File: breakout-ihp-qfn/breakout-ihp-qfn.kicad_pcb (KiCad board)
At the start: 4 copper layers, 50 x 50 mm, 113 parts, among them J1 Conn_01x12, J2 DF12NB-60DS-0.5V_51, J3 DF12NB-50DS-0.5V_51, U1 AP2112K-1.2, U2 AP2112K-1.8, U3 TT_IHP_ASIC, U4 24LC02

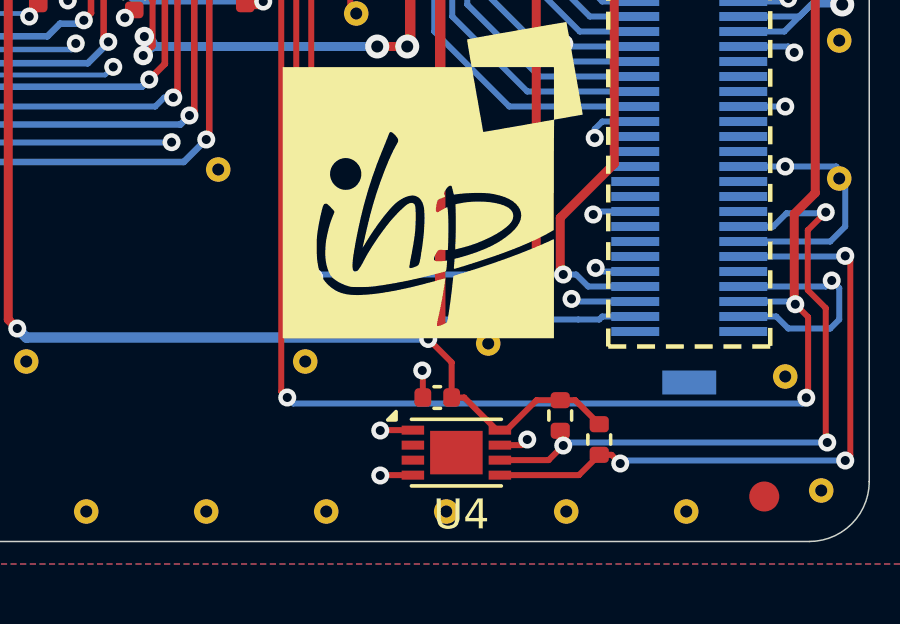
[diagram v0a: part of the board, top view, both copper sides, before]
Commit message: schem cleanup/project mux bus renames
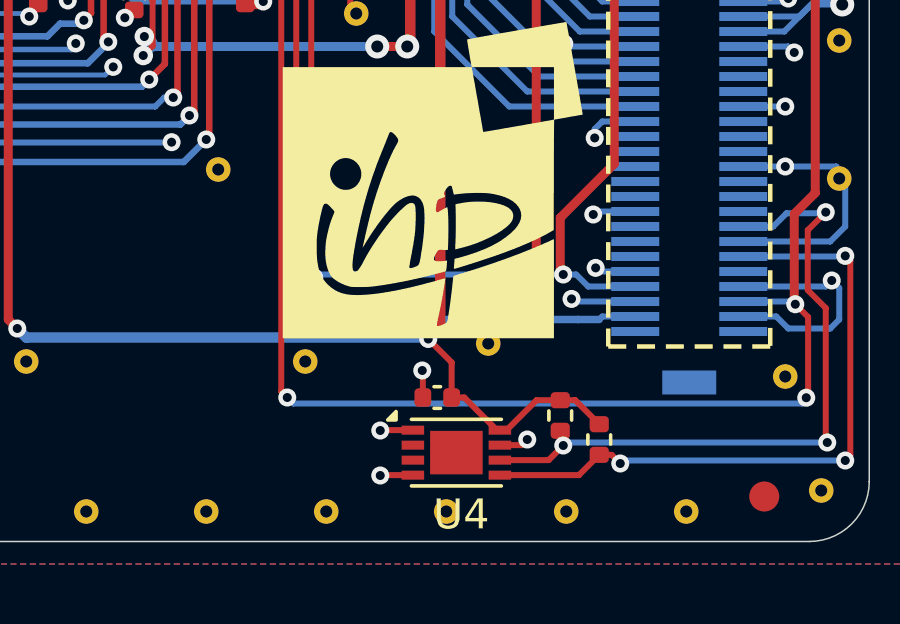
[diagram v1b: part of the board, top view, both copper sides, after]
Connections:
- net /c_ena renamed /enable
- net /c_rst_n renamed /rst_n
- net /c_sel_inc renamed /increment
- net /p_rst renamed /~{p_rst}

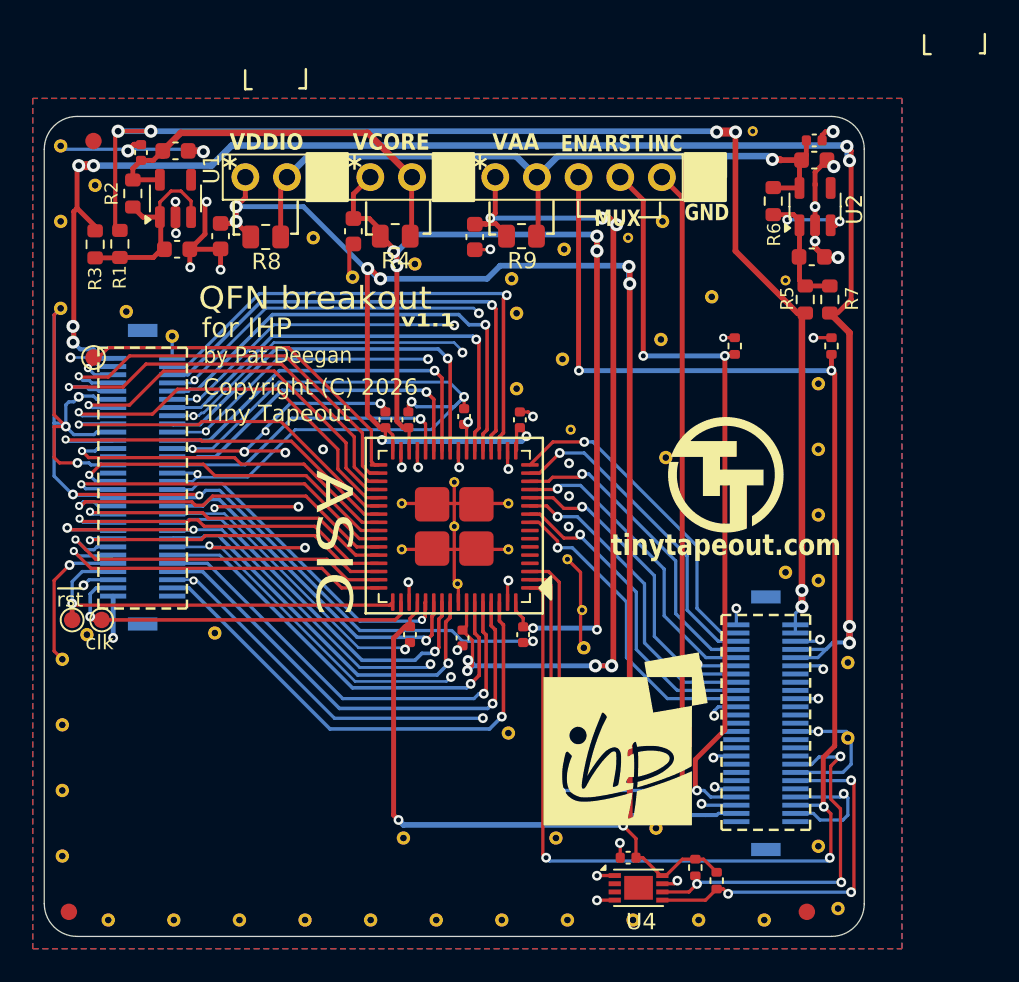
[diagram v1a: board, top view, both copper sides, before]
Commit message: PDN and other minor layout touchups
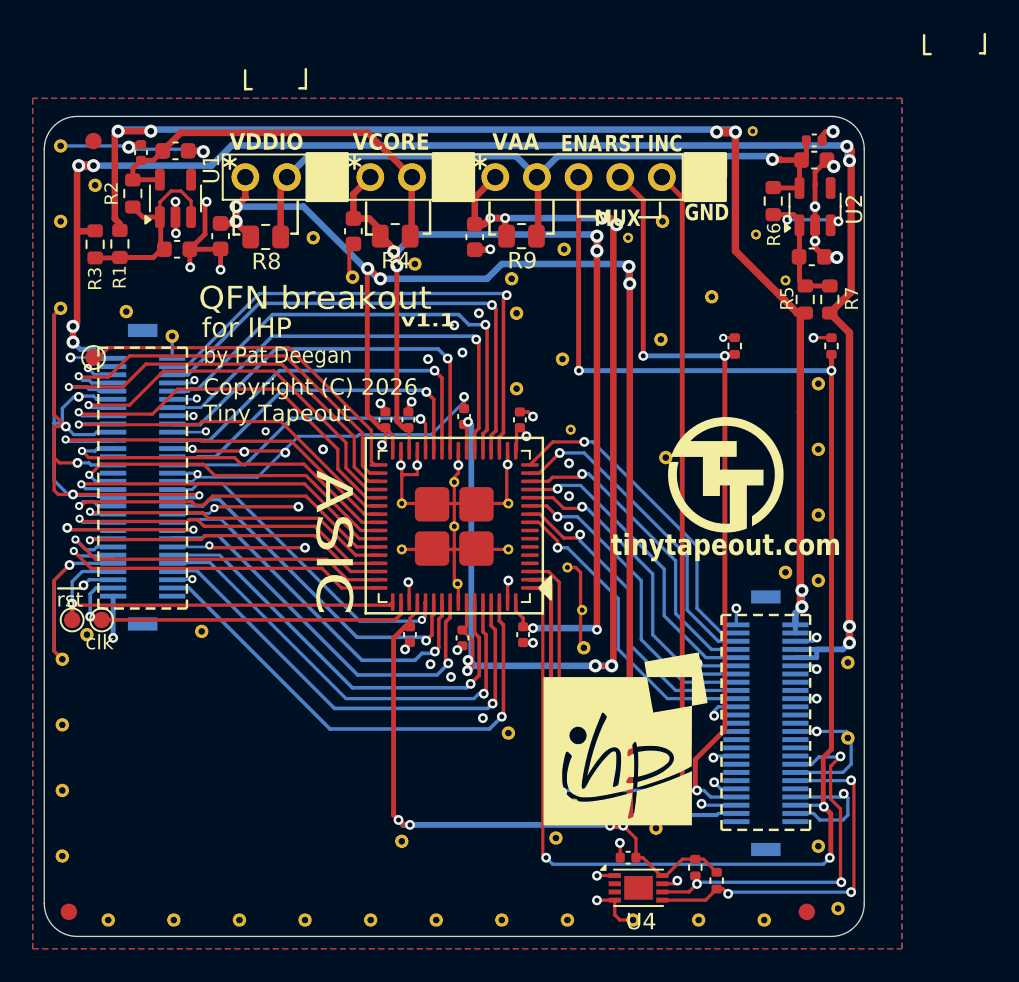
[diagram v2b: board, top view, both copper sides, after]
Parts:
- added STITCHSM01: StitchingVia-0.3mm, flyingcarsfootprints:StitchingVia-0.3mm, F.Cu at (156.4, 56.2)
- moved STITCH01 0.81 mm to (122.6, 80.4)
- moved STITCHSM01 0.50 mm to (144.9, 76.5)
- moved STITCHSM01 0.30 mm to (145.3, 90.9)
- moved STITCH01 0.22 mm to (134.8, 93.2)
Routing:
- net GND: track 436.0 -> 255.2 mm
- net VDD_{IO}: track 135.8 -> 141.1 mm, vias 10 -> 12
- net VAA: track 79.3 -> 81.7 mm, vias 8 -> 9
- net +3V3: track 112.7 -> 110.4 mm
